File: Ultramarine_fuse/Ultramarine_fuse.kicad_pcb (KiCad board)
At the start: 2 copper layers, 152.5 x 126 mm, 123 parts, among them J1 Conn_01x04_Female, J2 Conn_01x04_Female, SW1 SW_Push, SW10 SW_Push, SW11 SW_Push, SW12 SW_Push, SW13 SW_Push, SW14 SW_Push, SW15 SW_Push, SW16 SW_Push, SW17 SW_Push, SW18 SW_Push, SW19 SW_Push, SW2 SW_Push, SW20 SW_Push, SW21 SW_Push, SW22 SW_Push, SW23 SW_Push, SW24 SW_Push, SW25 SW_Push, SW26 SW_Push, SW27 SW_Push, SW28 SW_Push, SW29 SW_Push, SW3 SW_Push, SW30 SW_Push, SW31 SW_Push, SW32 SW_Push, SW33 SW_Push, SW34 SW_Push, SW35 SW_Push, SW36 SW_Push, SW4 SW_Push, SW5 SW_Push, SW6 SW_Push, SW7 SW_Push, SW8 SW_Push, SW9 SW_Push, U1 Pro_Micro, U10 SK6812mini, U11 SK6812mini, U12 SK6812mini, U13 SK6812mini, U14 SK6812mini, U15 SK6812mini, U16 SK6812mini, U17 SK6812mini, U18 SK6812mini, U19 SK6812mini, U2 SK6812mini, U20 SK6812mini, U21 SK6812mini, U22 SK6812mini, U23 SK6812mini, U24 SK6812mini, U25 SK6812mini, U26 SK6812mini, U27 SK6812mini, U28 SK6812mini, U29 SK6812mini, U3 SK6812mini, U30 SK6812mini, U31 SK6812mini, U32 SK6812mini, U33 SK6812mini, U34 SK6812mini, U35 SK6812mini, U36 SK6812mini, U4 SK6812mini, U5 SK6812mini, U6 SK6812mini, U7 SK6812mini, U8 SK6812mini, U9 SK6812mini

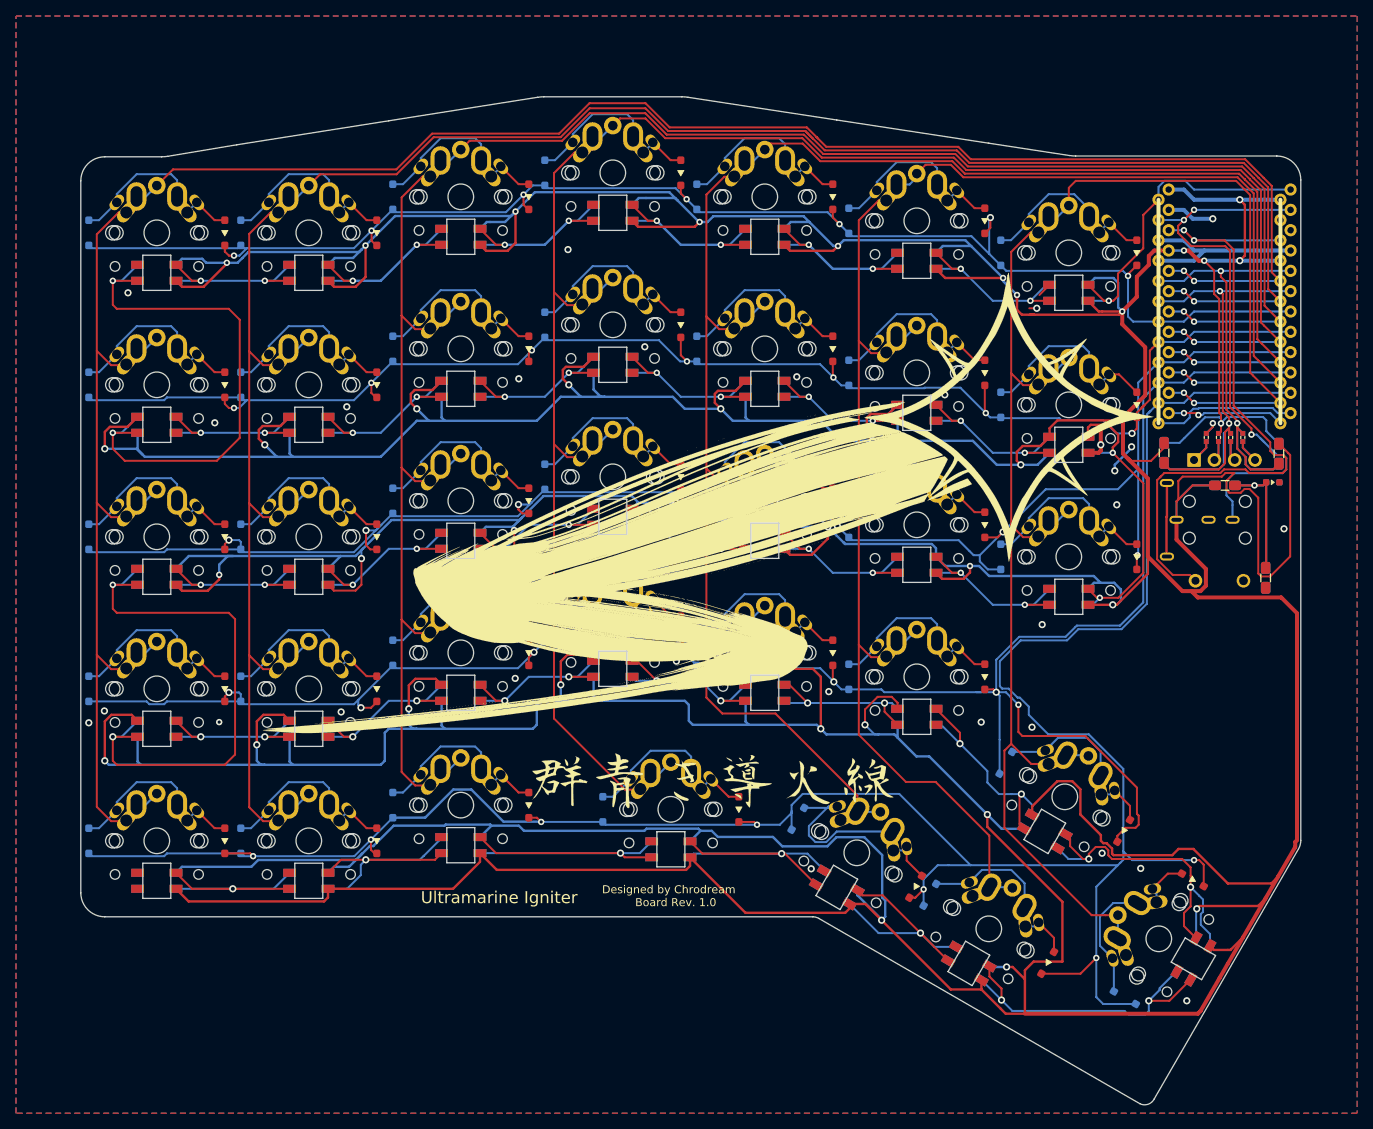
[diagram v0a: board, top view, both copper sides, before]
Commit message: fixed charge circuit for TP4056
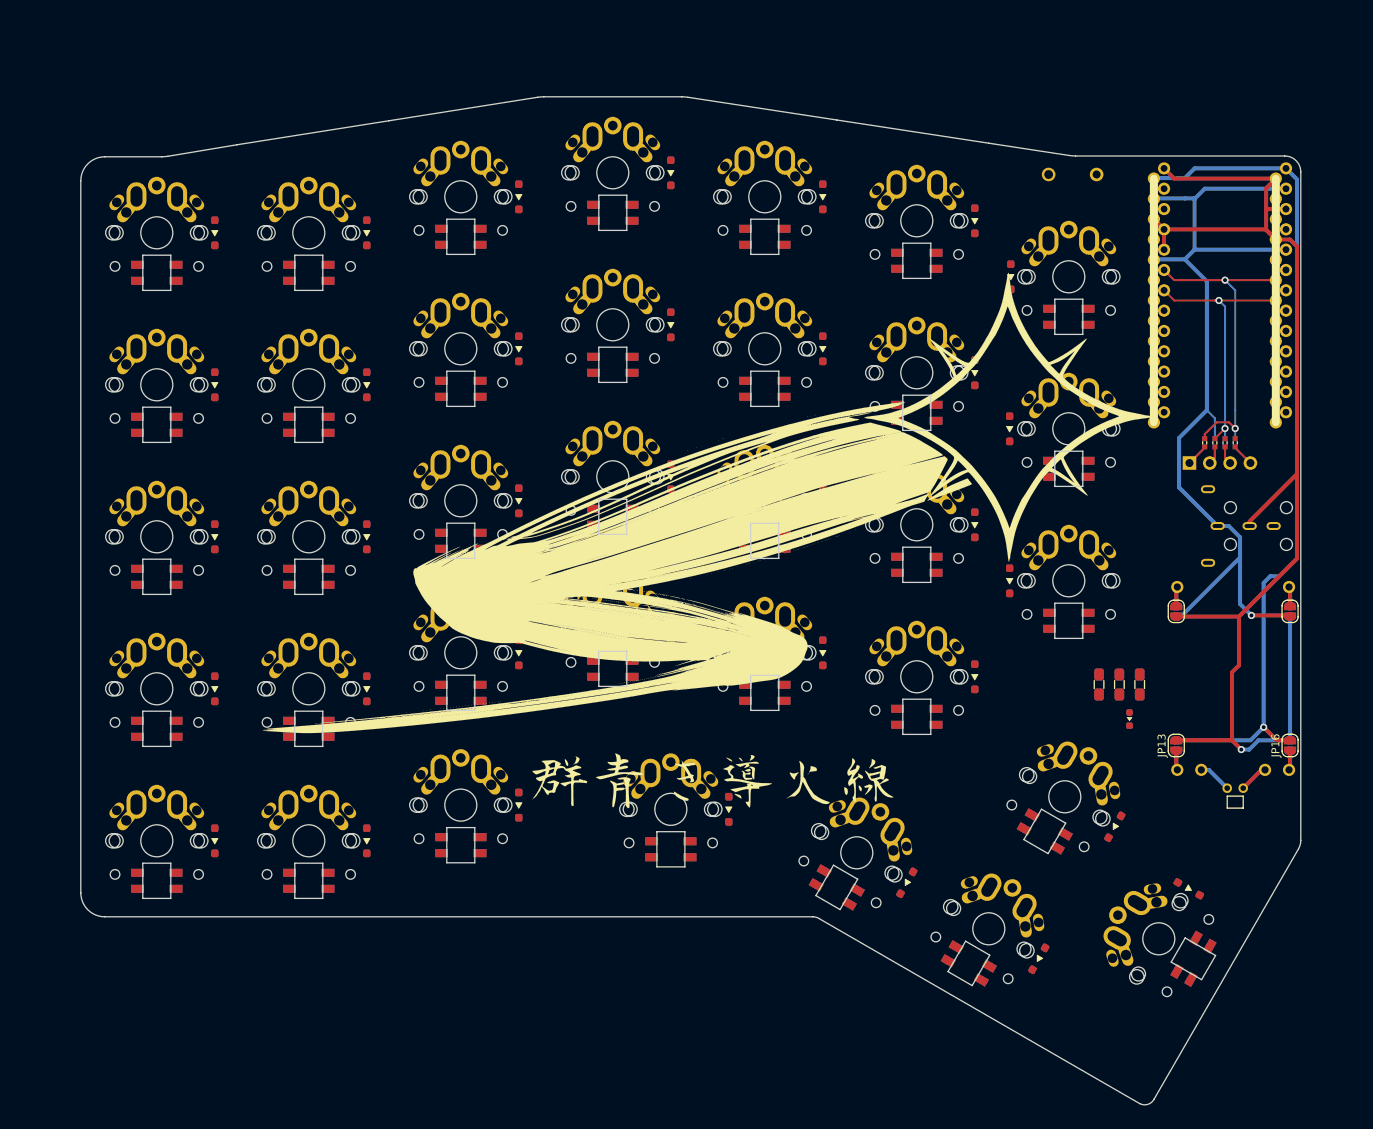
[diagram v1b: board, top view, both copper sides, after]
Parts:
- removed R1: R, Basic_SOP:1608
- added J3: Conn_01x02_Female, Basic_THT:S2B-PH-K-S, F.Cu at (177.8, 121.9)
- added JP10: Jumper, Jumper:SolderJumper-2_P1.3mm_Open_RoundedPad1.0x1.5mm, F.Cu at (184.7, 99.8)
- added JP11: Jumper, Jumper:SolderJumper-2_P1.3mm_Open_RoundedPad1.0x1.5mm, F.Cu at (170.4, 99.8)
- added JP12: Jumper, Jumper:SolderJumper-2_P1.3mm_Open_RoundedPad1.0x1.5mm, B.Cu at (184.7, 99.8)
- added JP13: Jumper, Jumper:SolderJumper-2_P1.3mm_Open_RoundedPad1.0x1.5mm, F.Cu at (170.4, 116.6)
- added JP14: Jumper, Jumper:SolderJumper-2_P1.3mm_Open_RoundedPad1.0x1.5mm, B.Cu at (170.4, 116.6)
- added JP15: Jumper, Jumper:SolderJumper-2_P1.3mm_Open_RoundedPad1.0x1.5mm, B.Cu at (184.7, 116.6)
- added JP16: Jumper, Jumper:SolderJumper-2_P1.3mm_Open_RoundedPad1.0x1.5mm, F.Cu at (184.7, 116.6)
- added JP9: Jumper, Jumper:SolderJumper-2_P1.3mm_Open_RoundedPad1.0x1.5mm, B.Cu at (170.4, 99.8)
- added U37: TP4056, Basic_THT:TP4056, B.Cu at (177.5, 108.2)
- R10: renamed from R4; value R -> 10K
- R8: renamed from R2; value R -> 330
- R9: renamed from R3; value R -> 10K
- U1: value Pro_Micro -> BLE-Micro-Pro; footprint ATMega:Pro-Micro -> ATMega:BLE-Micro-Pro
- moved SW36 54.0 mm to (157.5, 45.2), turned to 0 degrees
- moved D36 34.6 mm to (164.6, 113.3), turned to 270 degrees
- moved R9 33.7 mm to (165.9, 109.0)
- moved R10 30.1 mm to (160.8, 109.0)
- moved R8 28.2 mm to (163.3, 109.0), turned to 270 degrees
- moved D14 7.98 mm to (149.6, 77.0), turned to 90 degrees
- moved D21 7.98 mm to (149.6, 96.0), turned to 90 degrees
- moved D7 7.85 mm to (149.8, 58.0), turned to 90 degrees
- moved D28 7.29 mm to (162.8, 126.8), turned to 60 degrees
- moved D33 7.29 mm to (136.8, 133.8), turned to 60 degrees
- moved D34 7.29 mm to (153.2, 143.2), turned to 60 degrees
- moved D35 7.29 mm to (172.0, 134.5), turned to 150 degrees
- moved D1 7.25 mm to (50.2, 52.5), turned to 90 degrees
- moved D10 7.25 mm to (88.2, 67.0), turned to 90 degrees
- moved D11 7.25 mm to (107.2, 64.0), turned to 90 degrees
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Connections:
- JP1 pad 2: Net-(J1-Pad1) -> Net-(J1-Pad4)
- JP2 pad 2: Net-(J1-Pad2) -> Net-(J1-Pad3)
- JP3 pad 2: Net-(J1-Pad3) -> Net-(J1-Pad2)
- JP4 pad 2: Net-(J1-Pad4) -> Net-(J1-Pad1)
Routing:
- net VCC: track 1498.6 -> 112.0 mm, vias 37 -> 1
- net /Row4: track 309.2 -> 0.00 mm, vias 7 -> 0
- net /Col0: track 297.4 -> 0.00 mm, vias 2 -> 0
- net /Col1: track 280.9 -> 0.00 mm, vias 2 -> 0
- net /Col2: track 260.1 -> 0.00 mm, vias 2 -> 0
- net /Row3: track 250.2 -> 0.00 mm, vias 7 -> 0
- net /Col3: track 247.8 -> 0.00 mm, vias 2 -> 0
- net /Col4: track 235.1 -> 0.00 mm, vias 2 -> 0
- net /Col5: track 220.9 -> 0.00 mm, vias 2 -> 0
- net /Row2: track 211.7 -> 0.00 mm, vias 7 -> 0
- net /Col6: track 205.1 -> 0.00 mm, vias 2 -> 0
- net /Row1: track 187.1 -> 0.00 mm, vias 7 -> 0
- net /Row0: track 186.1 -> 0.00 mm, vias 7 -> 0
- net GND: track 43.4 -> 162.6 mm, vias 30 -> 1
- net /Bat+: track 0.00 -> 105.4 mm, vias 0 -> 1
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- removed copper zone on B.Cu, net GND
- removed copper zone on F.Cu, net GND
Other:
- outline, holes or cut-outs redrawn
- board text removed: "Designed by Chrodream ~ Board Rev. 1.0"
- board text removed: "Ultramarine Igniter"
